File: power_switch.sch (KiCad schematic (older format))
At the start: 111 parts, among them IC1 ATTINY2313A-P, P1 CONN_2, P10 CONN_01X01, P11 CONN_02X01, P12 CONN_01X01, P13 CONN_2, P14 CONN_2, P15 CONN_2, P16 CONN_2, P17 CONN_2, P18 CONN_2, P19 CONN_2, P2 CONN_2, P20 CONN_2, P21 CONN_01X03, P3 CONN_2, P4 CONN_2, P5 CONN_2, P6 CONN_01X03, P7 CONN_01X01, P8 CONN_01X01, P9 CONN_01X01, Q1 Q_NPN_EBC, Q10 Q_NJFET_DGS, Q11 Q_NPN_EBC, Q12 Q_NPN_EBC, Q13 Q_NJFET_DGS, Q14 Q_NJFET_DGS, Q2 Q_NJFET_DGS, Q3 Q_NPN_EBC, Q4 Q_NPN_EBC, Q5 Q_NJFET_DGS, Q6 Q_NJFET_DGS, Q7 Q_NPN_EBC, Q8 Q_NPN_EBC, Q9 Q_NJFET_DGS, U1 LTV-817, U2 LTV-817, U3 LTV-817, U4 LTV-817, U5 LTV-817, U6 LM317T, U7 LTV-817, U8 LTV-817, U9 LTV-817

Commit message: simplified version
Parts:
- removed JP10: Jumper_NO_Small, Buttons_Switches_ThroughHole:SW_PUSH_6mm, symbol Jumper_NO_Small
- removed P4: CONN_2, borniers:bornier2_V, symbol CONN_2-RESCUE-power_switch
- added 0.1, 0.? (x5), R?: R, symbol R
- added C? (x2): 10uF, symbol CP
- added C? (x2): 100n, symbol C
- added D?: 5v6, symbol D_Zener
- added D? (x5): D, Diodes_ThroughHole:Diode_DO-35_SOD27_Horizontal_RM10, symbol D
- added JP?: Jumper_NO_Small, symbol Jumper_NO_Small
- added P23: CONN_01X09, Socket_Strips:Socket_Strip_Straight_1x09, symbol CONN_01X09
- added P? (x5): CONN_2, borniers:bornier2_V, symbol CONN_2-RESCUE-power_switch
- added P? (x3): CONN_02X01, Pin_Headers:Pin_Header_Straight_1x02, symbol CONN_02X01
- added Q? (x5): Q_NJFET_DGS, TO_SOT_Packages_THT:TO-220_Neutral123_Vertical_LargePads, symbol Q_NJFET_DGS
- added R32, R33, R34, R35, R36, R37, R38, R39: 150R, Resistors_ThroughHole:Resistor_Horizontal_RM7mm, symbol R
- added RV?: POT, symbol POT
- added U?: LM358, symbol LM358
- P22: renamed from P?; footprint (none) -> Socket_Strips:Socket_Strip_Straight_1x09
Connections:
- net labels added: sw_S
- net labels removed: ts10
- wire segments 249 -> 324
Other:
- moved on the sheet: D1, P20, P22, P6, R1, R11, R18, R20, R26, R28, R31, R9

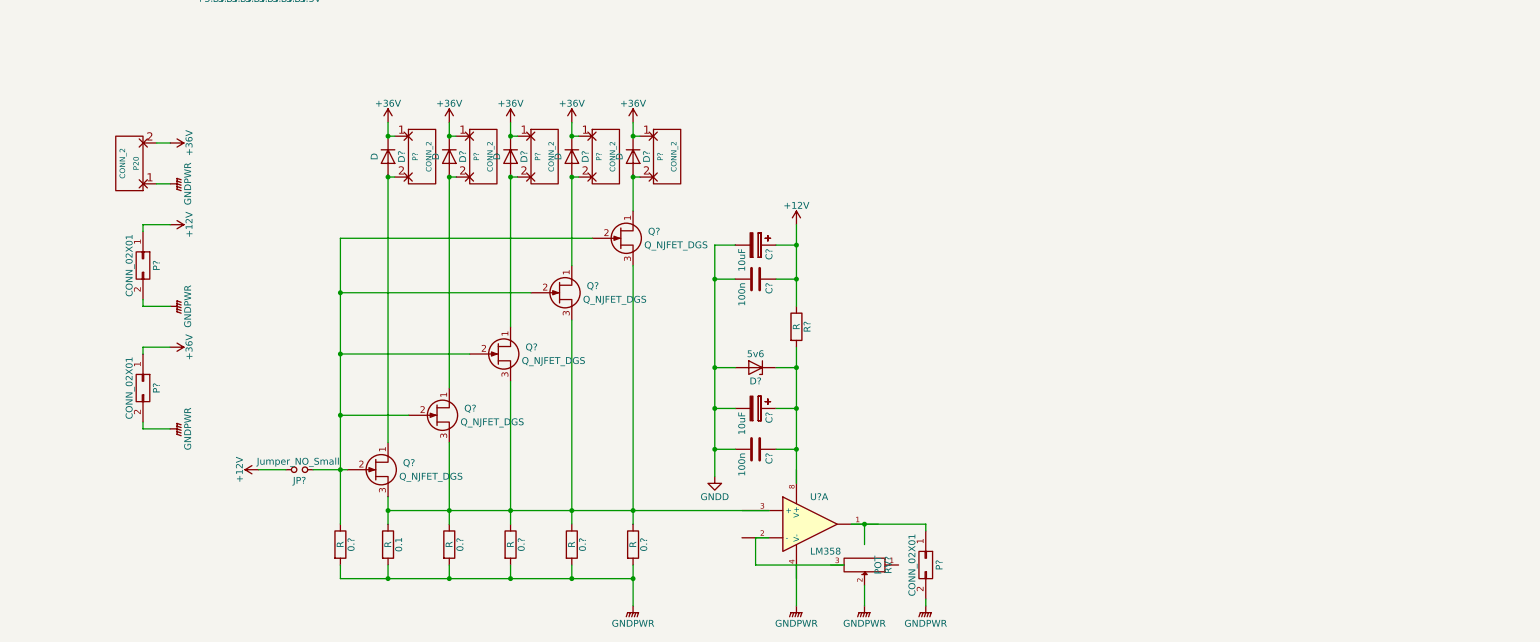
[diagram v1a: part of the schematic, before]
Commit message: working simple switch - no base version removed
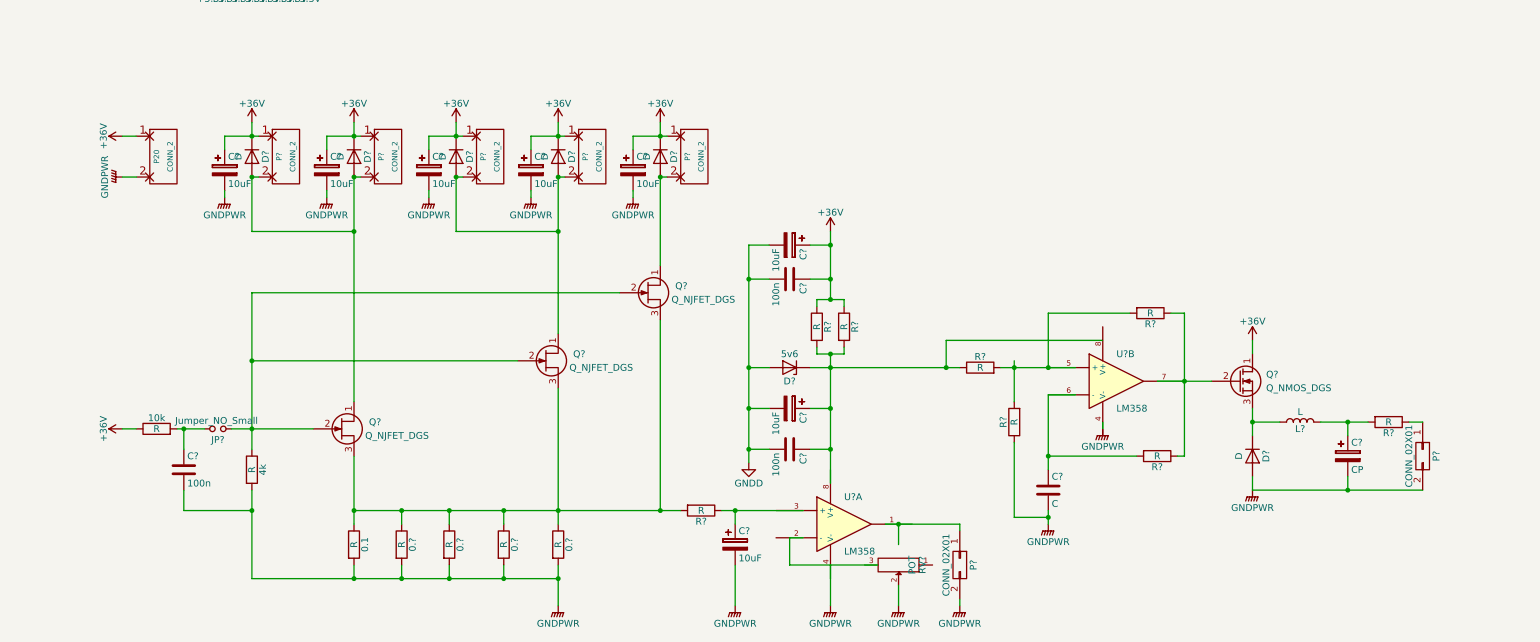
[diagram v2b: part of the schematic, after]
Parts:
- removed 0.?: R, symbol R
- removed P? (x2): CONN_02X01, Pin_Headers:Pin_Header_Straight_1x02, symbol CONN_02X01
- removed Q? (x2): Q_NJFET_DGS, TO_SOT_Packages_THT:TO-220_Neutral123_Vertical_LargePads, symbol Q_NJFET_DGS
- added 10k, 4k, R? (x7): R, symbol R
- added C? (x6): 10uF, symbol CP
- added C?: C, symbol C
- added C?: 100n, symbol C
- added C?: CP, symbol CP
- added D?: D, symbol D
- added L?: L, symbol L
- added P?: CONN_02X01, Pin_Headers:Pin_Header_Straight_1x02, symbol CONN_02X01
- added Q?: Q_NMOS_DGS, symbol Q_NMOS_DGS
- added U?: LM358, symbol LM358
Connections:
- wire segments 324 -> 366
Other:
- moved on the sheet: 0.1, 0.?, C?, D?, JP?, P20, P?, Q?, R?, RV?, U?A

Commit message: shematic for power and logic circuit
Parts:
- added 10k?, 4k?, R? (x2): R, symbol R
- added C? (x3): 10uF, symbol CP
- added C?: 100n, symbol C
- added JP?: Jumper_NO_Small, symbol Jumper_NO_Small
- added P? (x4): CONN_2, borniers:bornier2_V, symbol CONN_2-RESCUE-power_switch
- added P? (x2): CONN_02X01, Pin_Headers:Pin_Header_Straight_1x02, symbol CONN_02X01
- added Q? (x2): Q_NJFET_DGS, TO_SOT_Packages_THT:TO-220_Neutral123_Vertical_LargePads, symbol Q_NJFET_DGS
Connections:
- net labels added: +5V
- wire segments 366 -> 405

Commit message: versin with buck converter for amp meter backup
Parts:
- removed 0.1, 0.? (x4): R, symbol R
- removed 1k1, 2k1: R, Resistors_ThroughHole:Resistor_Horizontal_RM7mm, symbol R
- removed C1: 100n, Capacitors_ThroughHole:C_Disc_D3_P2.5, symbol C_Small
- removed C2: 4.7u, Capacitors_ThroughHole:C_Radial_D5_L11_P2, symbol CP1_Small
- removed C3, C5: C_Small, Capacitors_ThroughHole:C_Disc_D3_P2.5, symbol C_Small
- removed C4: 47uf, Capacitors_ThroughHole:C_Radial_D5_L11_P2, symbol CP1_Small
- removed C6: 4.7uF, Capacitors_ThroughHole:C_Radial_D5_L11_P2, symbol CP1_Small
- removed C7: 220uF, Capacitors_ThroughHole:C_Radial_D5_L11_P2, symbol CP1_Small
- removed D1, D10, D13, D14, D15, D5, D6, D9: Led_Small, LEDs:LED-3MM, symbol Led_Small
- removed D11, D12, D2, D3, D4, D7, D8: D, Diodes_ThroughHole:Diode_DO-35_SOD27_Horizontal_RM10, symbol D
- removed IC1: ATTINY2313A-P, Housings_DIP:DIP-20_W7.62mm_LongPads, symbol ATTINY2313A-P
- removed JP1, JP2, JP3, JP4, JP5, JP6, JP7, JP8, JP9: Jumper_NO_Small, Buttons_Switches_ThroughHole:SW_PUSH_6mm, symbol Jumper_NO_Small
- removed P1, P13, P14, P15, P16, P17, P18, P19, P2, P3, P5: CONN_2, borniers:bornier2_V, symbol CONN_2-RESCUE-power_switch
- removed P10, P12, P7, P9: CONN_01X01, Mounting_Holes:MountingHole_3.2mm_M3_Pad, symbol CONN_01X01
- removed P11: CONN_02X01, Pin_Headers:Pin_Header_Straight_1x02, symbol CONN_02X01
- removed P21, P6: CONN_01X03, Pin_Headers:Pin_Header_Straight_1x03, symbol CONN_01X03
- removed P22, P23: CONN_01X09, Socket_Strips:Socket_Strip_Straight_1x09, symbol CONN_01X09
- removed P8: CONN_01X01, Pin_Headers:Pin_Header_Straight_1x01, symbol CONN_01X01
- removed Q1, Q11, Q12, Q3, Q4, Q7, Q8: Q_NPN_EBC, TO_SOT_Packages_THT:TO-92_Inline_Narrow_Oval, symbol Q_NPN_EBC
- removed Q10, Q13, Q14, Q2, Q5, Q6, Q9, Q? (x3): Q_NJFET_DGS, TO_SOT_Packages_THT:TO-220_Neutral123_Vertical_LargePads, symbol Q_NJFET_DGS
- removed R1, R18, R20, R26, R28, R31, R32, R33, R34, R35, R36, R37, R38, R39, R9: 150R, Resistors_ThroughHole:Resistor_Horizontal_RM7mm, symbol R
- removed R10, R19, R21, R27, R29, R4: 20k, Resistors_ThroughHole:Resistor_Horizontal_RM7mm, symbol R
- removed R16, R2, R22, R24, R30, R5, R7: 100k, Resistors_ThroughHole:Resistor_Horizontal_RM7mm, symbol R
- removed R17, R23, R25, R3, R6, R8: 68k, Resistors_ThroughHole:Resistor_Horizontal_RM7mm, symbol R
- removed U1, U2, U3, U4, U5, U7, U8, U9: LTV-817, Housings_DIP:DIP-4_W7.62mm_LongPads, symbol LTV-817
- removed U6: LM317T, Power_Integrations:TO-220, symbol LM317T
- added C9: 100n, Capacitors_ThroughHole:C_Disc_D3_P2.5, symbol C
- added Q2, Q3, Q5: IRF9540, TO_SOT_Packages_THT:TO-220_Neutral123_Vertical_LargePads, symbol Q_NJFET_GSD
- C1, C2, C3, C4, C5, C6, C8: renamed from C?; footprint (none) -> Capacitors_ThroughHole:C_Radial_D10_L20_P7.5
- C10, C12, C13, C18, C7: renamed from C?; footprint (none) -> Capacitors_ThroughHole:C_Disc_D3_P2.5
- C11: renamed from C?; value CP -> 10uF; footprint (none) -> Capacitors_ThroughHole:C_Radial_D8_L13_P3.8
- C14, C15, C16, C17: renamed from C?; footprint (none) -> Capacitors_ThroughHole:C_Radial_D8_L11.5_P3.5
- D6: renamed from D?; footprint (none) -> Diodes_ThroughHole:Diode_DO-35_SOD27_Horizontal_RM10
- D7: renamed from D?; value D -> 1N4001; footprint (none) -> Diodes_ThroughHole:Diode_DO-35_SOD27_Horizontal_RM10
- JP1, JP2: renamed from JP?; footprint (none) -> Pin_Headers:Pin_Header_Angled_1x02_Pitch1.27mm
- L1: renamed from L?; value L -> 50uH; footprint (none) -> Choke_Axial_ThroughHole:Choke_Horizontal_RM10mm
- P13, P6, P7, P8: renamed from P?; footprint Pin_Headers:Pin_Header_Straight_1x02 -> Socket_Strips:Socket_Strip_Straight_2x01
- Q1: renamed from Q?; value Q_NJFET_DGS -> 2N7000
- Q4: renamed from Q?; footprint (none) -> TO_SOT_Packages_THT:TO-92_Inline_Narrow_Oval
- Q6: renamed from Q?; value Q_NJFET_DGS -> 2N7000; footprint TO_SOT_Packages_THT:TO-220_Neutral123_Vertical_LargePads -> TO_SOT_Packages_THT:TO-92_Inline_Narrow_Oval
- R1, R2, R3, R5, R6, R8, R9: renamed from R?; footprint (none) -> Resistors_ThroughHole:Resistor_Horizontal_RM7mm
- R10: renamed from R?; value R -> 60k; footprint (none) -> Resistors_ThroughHole:Resistor_Horizontal_RM7mm
- R11: value 150R -> 0.1R; footprint Resistors_ThroughHole:Resistor_Horizontal_RM7mm -> Resistors_ThroughHole:Resistor_Vertical_RM5mm
- R12: value 20k -> 0.1R; footprint Resistors_ThroughHole:Resistor_Horizontal_RM7mm -> Resistors_ThroughHole:Resistor_Vertical_RM5mm
- R13: value R -> 0.1R; footprint Resistors_ThroughHole:Resistor_Horizontal_RM7mm -> Resistors_ThroughHole:Resistor_Vertical_RM5mm
- R14: value 100k -> 0.1R; footprint Resistors_ThroughHole:Resistor_Horizontal_RM7mm -> Resistors_ThroughHole:Resistor_Vertical_RM5mm
- R15: value 68k -> 0.1R; footprint Resistors_ThroughHole:Resistor_Horizontal_RM7mm -> Resistors_ThroughHole:Resistor_Vertical_RM5mm
- R16: renamed from 10k; footprint (none) -> Resistors_ThroughHole:Resistor_Horizontal_RM7mm
- R17: renamed from 4k; footprint (none) -> Resistors_ThroughHole:Resistor_Horizontal_RM7mm
- R18: renamed from 10k?; value R -> 10k; footprint (none) -> Resistors_ThroughHole:Resistor_Horizontal_RM7mm
- R19: renamed from 4k?; value R -> 220R; footprint (none) -> Resistors_ThroughHole:Resistor_Horizontal_RM7mm
- R4, R7: renamed from R?; value R -> 220R; footprint (none) -> Resistors_ThroughHole:Resistor_Horizontal_RM7mm
- RV1: renamed from RV?; footprint (none) -> Potentiometers:Potentiometer_Bourns_3296X_3-8Zoll_Inline_ScrewFront
- U1: renamed from U?; footprint (none) -> Housings_DIP:DIP-8_W7.62mm_LongPads
- gave numbers to parts that had none: 14
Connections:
- net labels removed: +12V, +3.3V, +48V, GNDD, sw_E, sw_R, sw_S, sw_T, sw_U, sw_V, sw_X, sw_Y, ts1, ts2, ts3, ts4, ts5, ts6, ts7, ts8, ts9
- wire segments 405 -> 217
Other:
- note removed: "estop"
- note removed: "log"
- note removed: "r"
- note removed: "switch all off"
- note removed: "switch all on"
- note removed: "tool"
- note removed: "u"
- note removed: "v"
- note removed: "x"
- note removed: "y"
- moved on the sheet: C1, C10, C11, C12, C13, C14, C15, C16, C17, C18, C2, C3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

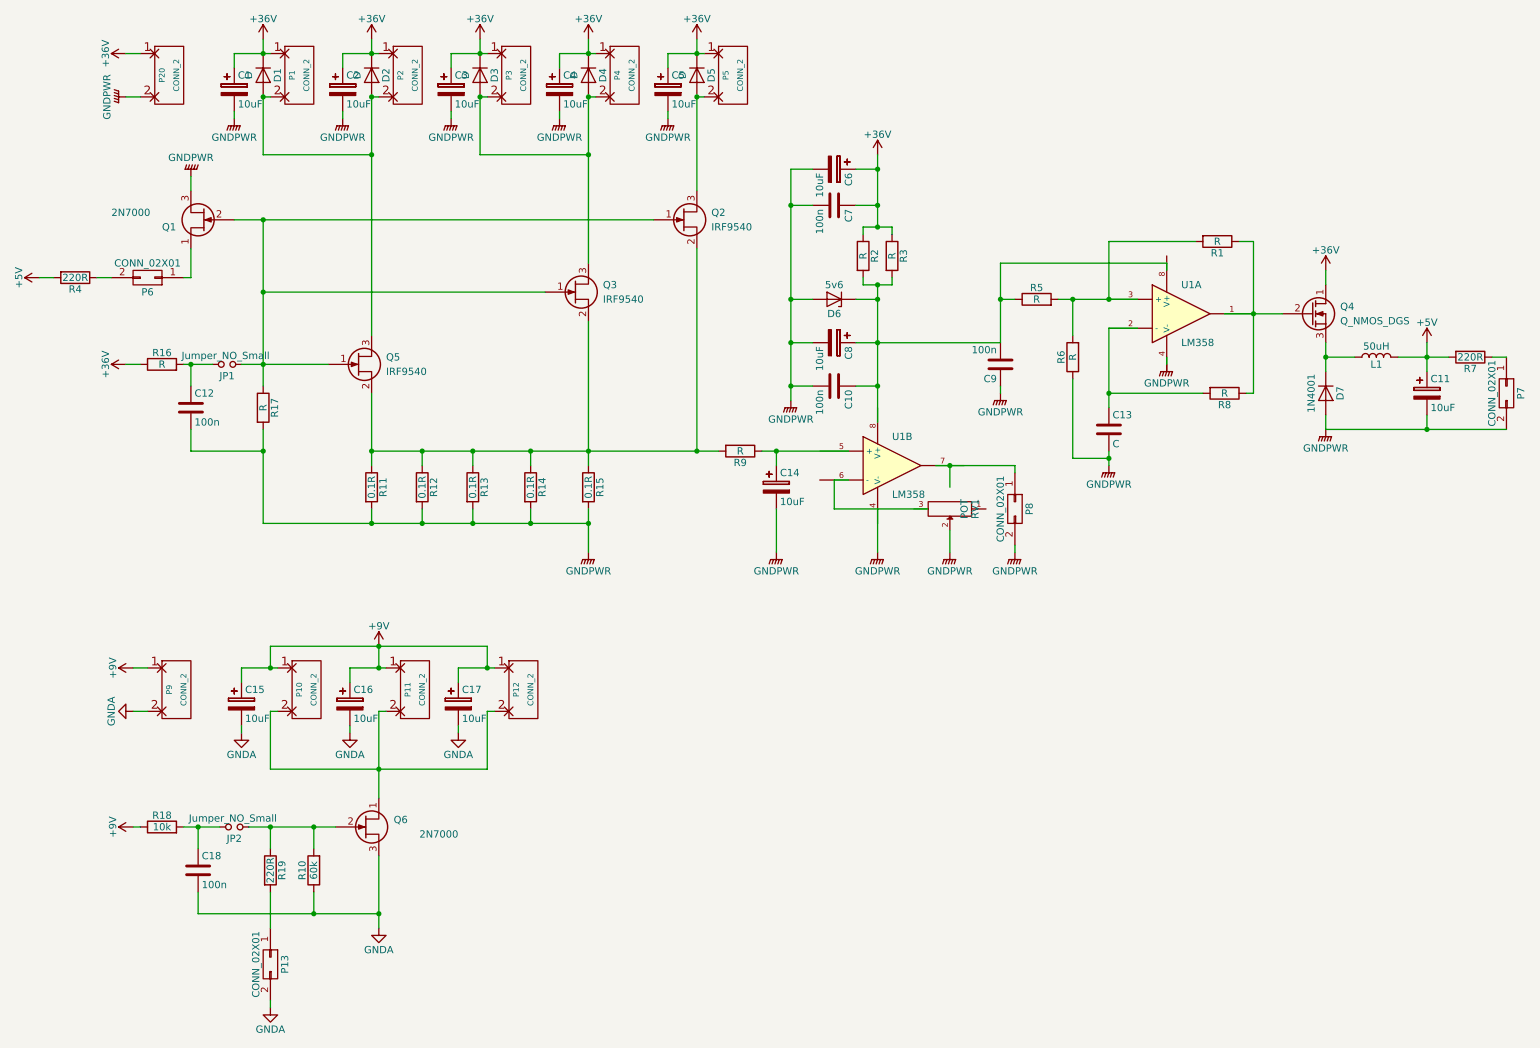
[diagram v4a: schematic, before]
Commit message: powerswitch with tracks
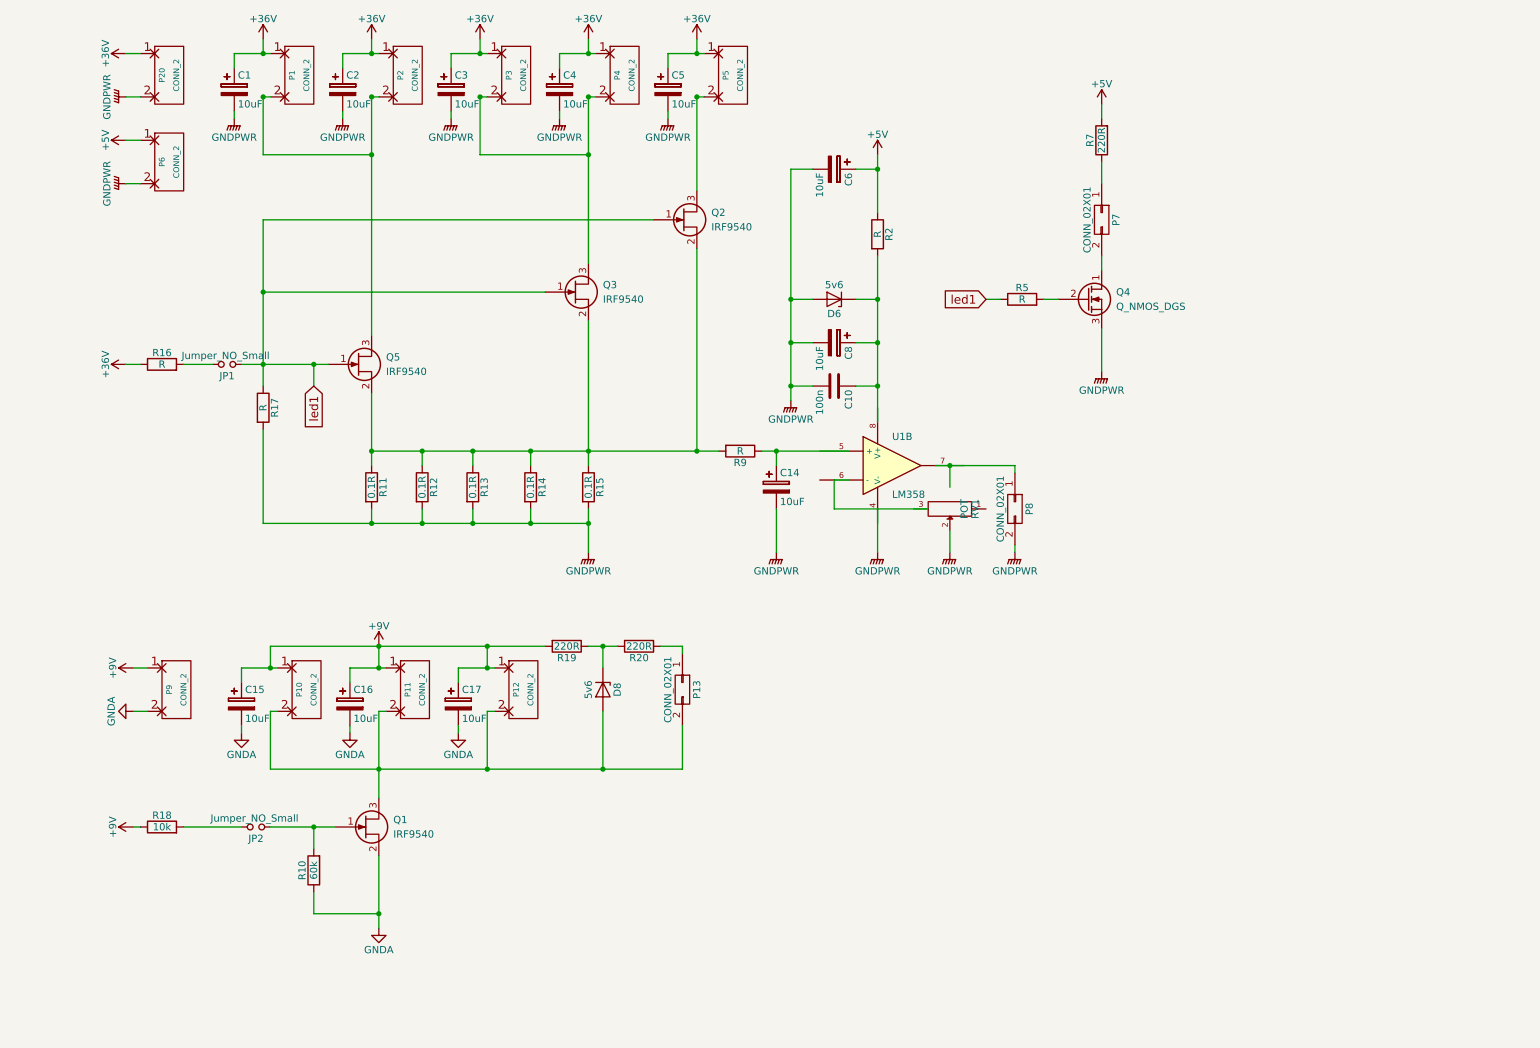
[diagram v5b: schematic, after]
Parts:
- removed C11: 10uF, Capacitors_ThroughHole:C_Radial_D8_L13_P3.8, symbol CP
- removed C12, C18, C7, C9: 100n, Capacitors_ThroughHole:C_Disc_D3_P2.5, symbol C
- removed C13: C, Capacitors_ThroughHole:C_Disc_D3_P2.5, symbol C
- removed D1, D2, D3, D4, D5: D, Diodes_ThroughHole:Diode_DO-35_SOD27_Horizontal_RM10, symbol D
- removed D7: 1N4001, Diodes_ThroughHole:Diode_DO-35_SOD27_Horizontal_RM10, symbol D
- removed L1: 50uH, Choke_Axial_ThroughHole:Choke_Horizontal_RM10mm, symbol L
- removed P6: CONN_02X01, Socket_Strips:Socket_Strip_Straight_2x01, symbol CONN_02X01
- removed Q1: 2N7000, TO_SOT_Packages_THT:TO-220_Neutral123_Vertical_LargePads, symbol Q_NJFET_DGS
- removed Q6: 2N7000, TO_SOT_Packages_THT:TO-92_Inline_Narrow_Oval, symbol Q_NJFET_DGS
- removed R1, R3, R6, R8: R, Resistors_ThroughHole:Resistor_Horizontal_RM7mm, symbol R
- removed R4: 220R, Resistors_ThroughHole:Resistor_Horizontal_RM7mm, symbol R
- removed unit 1 of U1
- added D8: 5v6, Diodes_ThroughHole:D_DO-35_SOD27_P7.62mm_Horizontal, symbol D_Zener
- added P6: CONN_2, borniers:bornier2_V, symbol CONN_2-RESCUE-power_switch
- added Q1: IRF9540, TO_SOT_Packages_THT:TO-220_Neutral123_Vertical_LargePads, symbol Q_NJFET_GSD
- added R20: 220R, Resistors_ThroughHole:R_Axial_DIN0207_L6.3mm_D2.5mm_P7.62mm_Horizontal, symbol R
- C6: footprint Capacitors_ThroughHole:C_Radial_D10_L20_P7.5 -> Capacitors_ThroughHole:CP_Radial_D6.3mm_P2.50mm
- C8: footprint Capacitors_ThroughHole:C_Radial_D10_L20_P7.5 -> Capacitors_ThroughHole:CP_Radial_D4.0mm_P2.00mm
- D6: footprint Diodes_ThroughHole:Diode_DO-35_SOD27_Horizontal_RM10 -> Diodes_ThroughHole:D_DO-35_SOD27_P7.62mm_Horizontal
- JP1, JP2: footprint Pin_Headers:Pin_Header_Angled_1x02_Pitch1.27mm -> Pin_Headers:Pin_Header_Straight_1x02_Pitch2.54mm
- R10, R16, R17, R18, R19, R2, R5, R7, R9: footprint Resistors_ThroughHole:Resistor_Horizontal_RM7mm -> Resistors_ThroughHole:R_Axial_DIN0207_L6.3mm_D2.5mm_P7.62mm_Horizontal
- R11, R12, R13, R14, R15: footprint Resistors_ThroughHole:Resistor_Vertical_RM5mm -> Resistors_ThroughHole:R_Axial_DIN0411_L9.9mm_D3.6mm_P5.08mm_Vertical
- RV1: footprint Potentiometers:Potentiometer_Bourns_3296X_3-8Zoll_Inline_ScrewFront -> Potentiometers:Potentiometer_Bourns_3296W_3-8Zoll_Inline_ScrewUp
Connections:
- net labels added: led1
- wire segments 217 -> 121
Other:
- moved on the sheet: JP2, P13, Q4, R19, R2, R5, R7
